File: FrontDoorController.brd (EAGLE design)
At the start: 31.4 x 49.1 mm, 10 parts

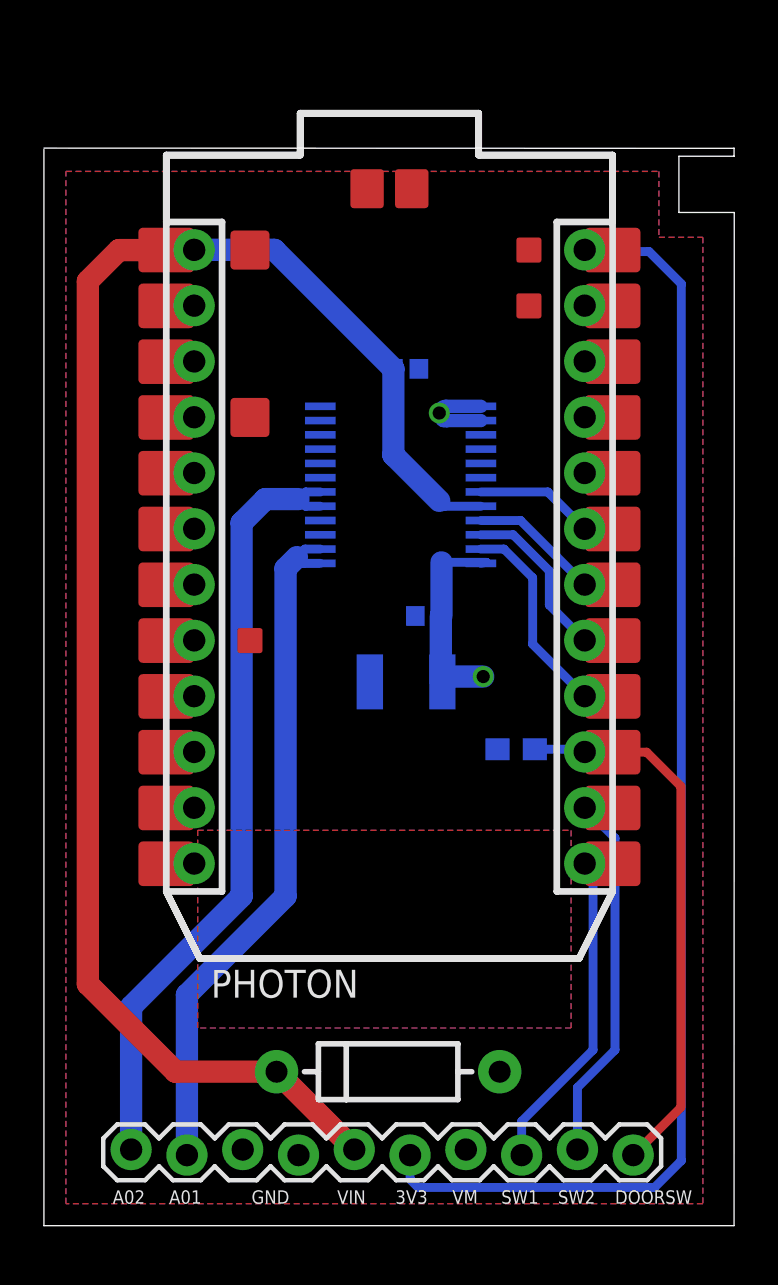
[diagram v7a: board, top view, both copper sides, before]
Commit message: Door_Control_PCB: Make the cutout a bit bigger
Make the cutout and tab for the slot that holds onto the Lockitron
mechanical assembly a bit bigger so that the fab will (hopefully) make
it.  The pictures from Sparkfun show this tab as being about 1/20th of
an inch or about 0.05 inches (about 50 mils).
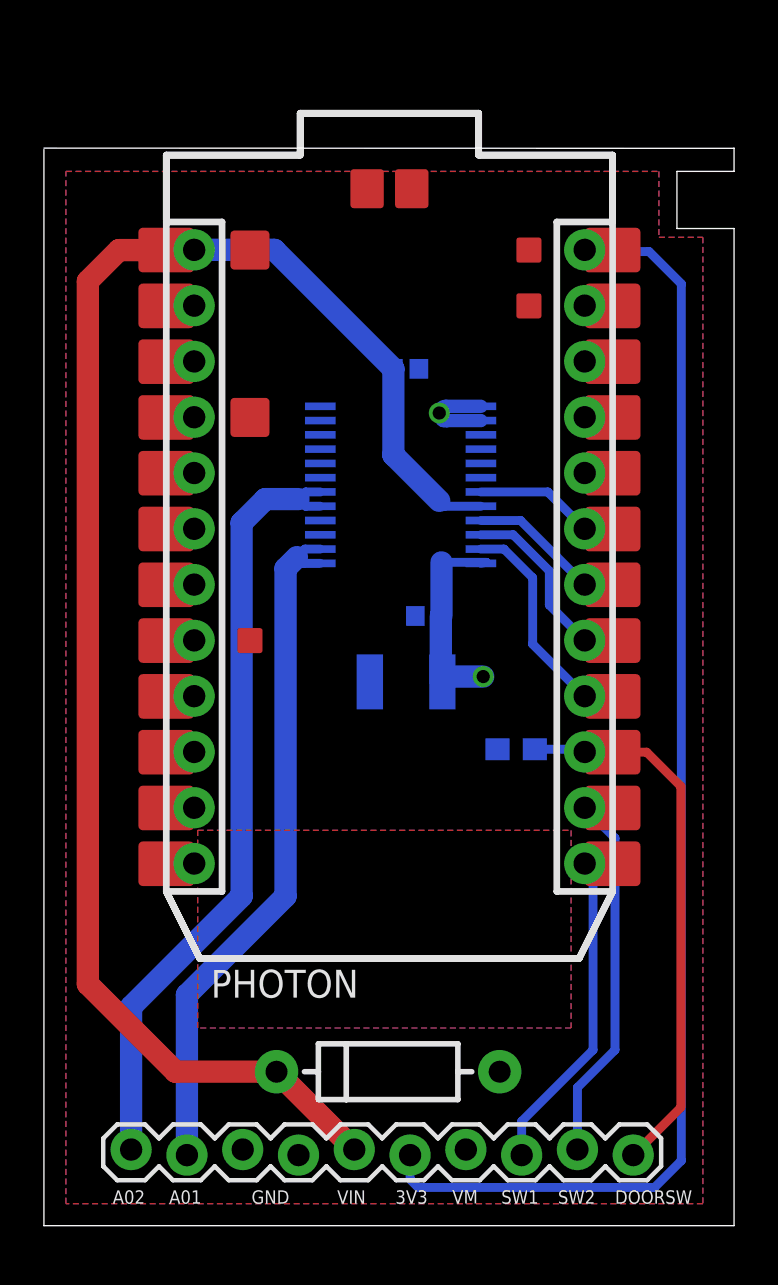
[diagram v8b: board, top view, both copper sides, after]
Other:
- outline, holes or cut-outs redrawn
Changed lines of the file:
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@@
 <plain>
 <wire x1="0" y1="0" x2="31.42" y2="0" width="0" layer="20"/>
-<wire x1="31.42" y1="0" x2="31.43" y2="46.13" width="0" layer="20"/>
-<wire x1="31.43" y1="46.13" x2="28.91" y2="46.13" width="0" layer="20"/>
-<wire x1="28.91" y1="46.13" x2="28.91" y2="48.69" width="0" layer="20"/>
-<wire x1="28.91" y1="48.69" x2="31.42" y2="48.69" width="0" layer="20"/>
-<wire x1="31.42" y1="48.69" x2="31.42" y2="49.05" width="0" layer="20"/>
+<wire x1="31.42" y1="0" x2="31.42" y2="45.4" width="0" layer="20"/>
+<wire x1="31.42" y1="45.4" x2="28.82" y2="45.4" width="0" layer="20"/>
+<wire x1="28.82" y1="45.4" x2="28.82" y2="48" width="0" layer="20"/>
+<wire x1="28.82" y1="48" x2="31.42" y2="48" width="0" layer="20"/>
+<wire x1="31.42" y1="48" x2="31.42" y2="49.05" width="0" layer="20"/>
 <wire x1="31.42" y1="49.05" x2="31.42" y2="49.06" width="0" layer="20"/>
 <wire x1="31.42" y1="49.05" x2="0" y2="49.06" width="0" layer="20"/>
-<dimension x1="31.42" y1="48.69" x2="28.91" y2="48.7" x3="30.1732375" y3="50.763453125" textsize="1.778" layer="48" unit="mil"/>
-<dimension x1="31.42" y1="48.69" x2="31.43" y2="46.13" x3="39.882878125" y3="47.4430375" textsize="1.778" layer="48" unit="mil"/>
 <wire x1="0" y1="0" x2="0" y2="49" width="0" layer="20"/>
 <dimension x1="0" y1="0" x2="0" y2="49" x3="-4" y3="24.5" textsize="1.778" layer="48" unit="inch"/>
@@
 <text x="23.4" y="1" size="0.6096" layer="25">SW2</text>
 <text x="26" y="1" size="0.6096" layer="25">DOORSW</text>
+<dimension x1="31.42" y1="49.05" x2="31.42" y2="48" x3="37" y3="48.525" textsize="0.6096" layer="25" unit="mil"/>
+<dimension x1="31.42" y1="45.4" x2="31.42" y2="48" x3="34" y3="46.7" textsize="0.6096" layer="25" unit="mil"/>
+<dimension x1="28.82" y1="48" x2="31.42" y2="48" x3="30.12" y3="54" textsize="0.6096" layer="25" unit="mil"/>
 </plain>
 <attributes>
